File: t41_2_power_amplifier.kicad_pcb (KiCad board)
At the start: 2 copper layers, 100 x 100 mm, 2 parts, among them Q1 Q_NMOS_GSD, Q3 Q_NMOS_GSD

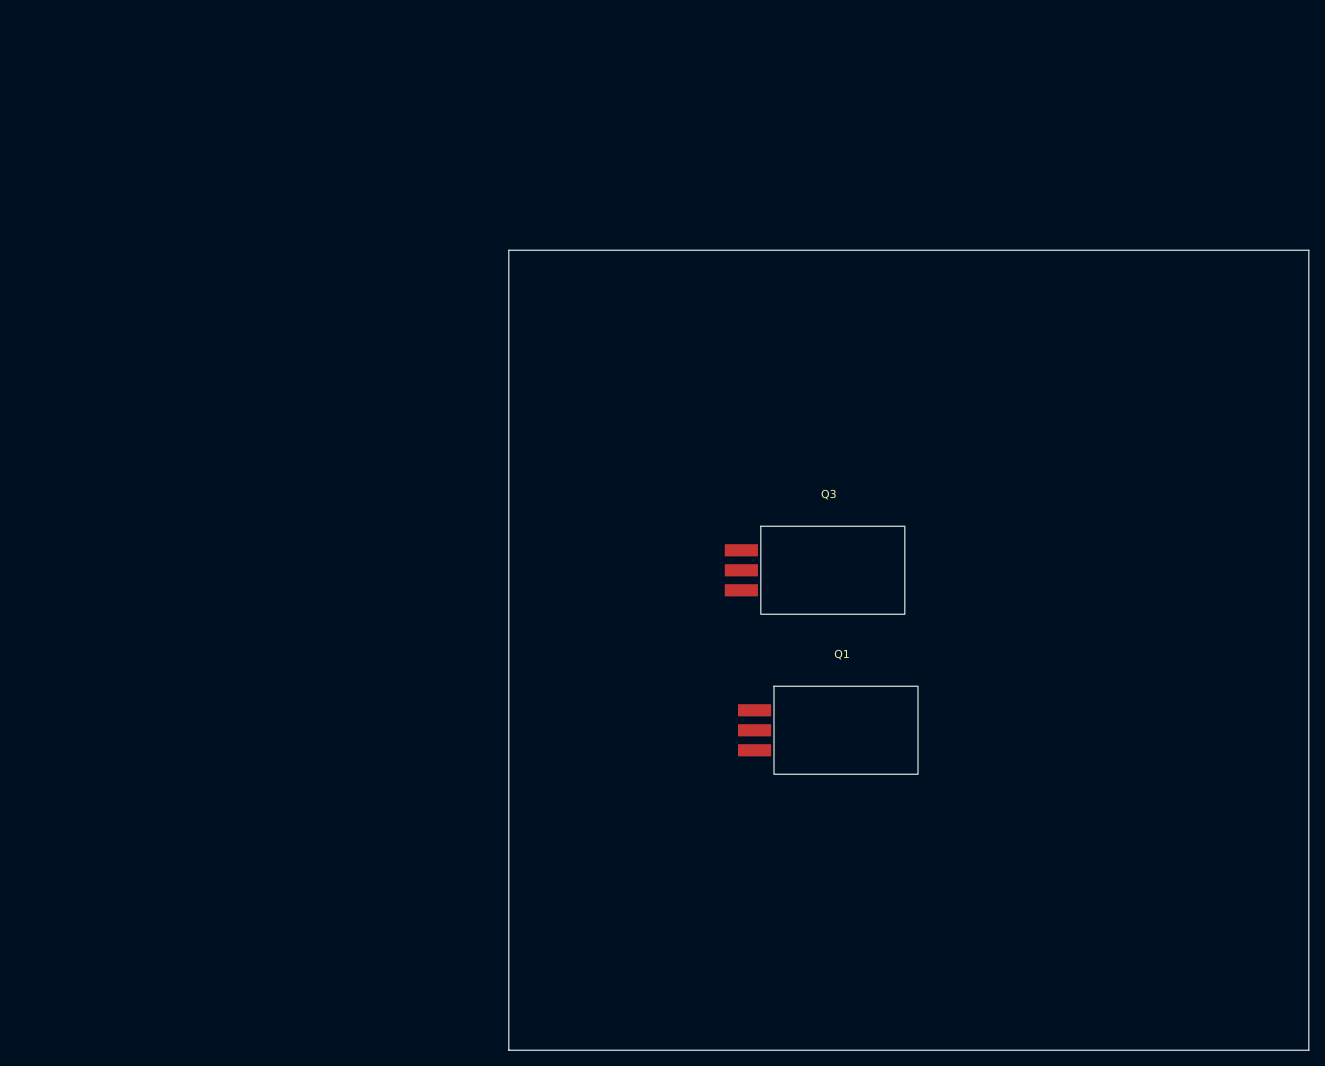
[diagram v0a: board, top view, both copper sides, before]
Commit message: Schematic complete, started on layout.
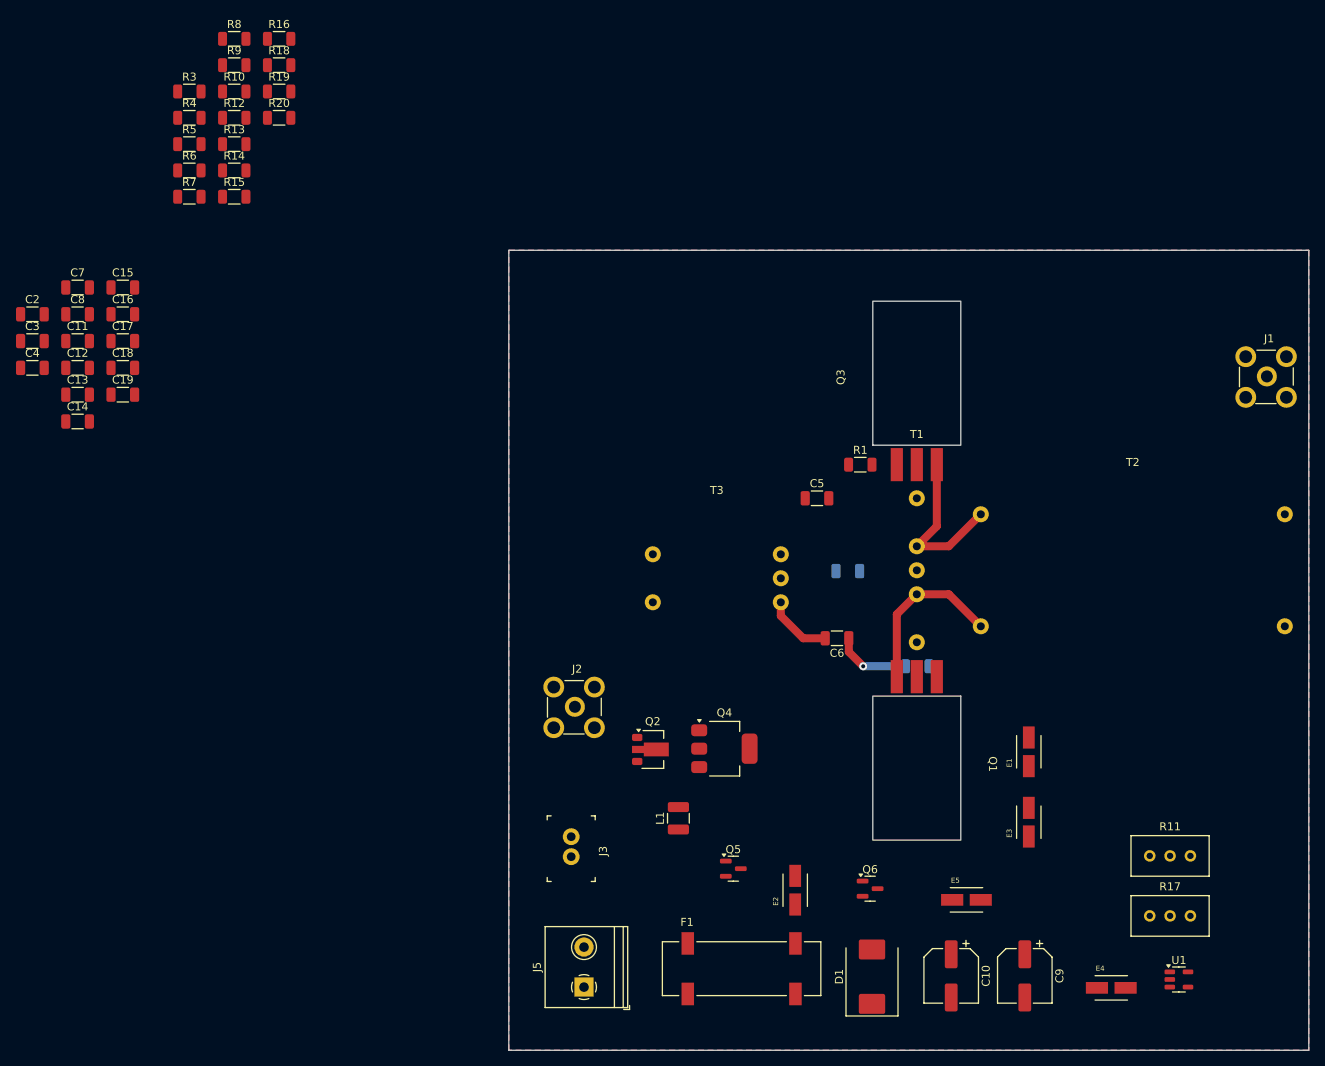
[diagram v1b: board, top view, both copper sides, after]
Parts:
- added C1: 0.1uF, Capacitor_SMD:C_1206_3216Metric, B.Cu at (142.4, 90.1)
- added C10: 47uF, Capacitor_SMD:CP_Elec_6.3x5.7, F.Cu at (155.3, 140.7)
- added C11: 0.1uF, Capacitor_SMD:C_1206_3216Metric, F.Cu at (46.1, 61.4)
- added C12: 0.1uF, Capacitor_SMD:C_1206_3216Metric, F.Cu at (46.1, 64.7)
- added C13: 0.1uF, Capacitor_SMD:C_1206_3216Metric, F.Cu at (46.1, 68.0)
- added C14: 0.1uF, Capacitor_SMD:C_1206_3216Metric, F.Cu at (46.1, 71.4)
- added C15: 0.1uF, Capacitor_SMD:C_1206_3216Metric, F.Cu at (51.8, 54.6)
- added C16: 0.1uF, Capacitor_SMD:C_1206_3216Metric, F.Cu at (51.8, 58.0)
- added C17: 0.1uF, Capacitor_SMD:C_1206_3216Metric, F.Cu at (51.8, 61.4)
- added C18: 1uF, Capacitor_SMD:C_1206_3216Metric, F.Cu at (51.8, 64.7)
- added C19: 0.1uF, Capacitor_SMD:C_1206_3216Metric, F.Cu at (51.8, 68.0)
- added C2: 180pF, Capacitor_SMD:C_1206_3216Metric, F.Cu at (40.5, 58.0)
- added C3: 0.1uF, Capacitor_SMD:C_1206_3216Metric, F.Cu at (40.5, 61.4)
- added C4: 0.1uF, Capacitor_SMD:C_1206_3216Metric, F.Cu at (40.5, 64.7)
- added C5: 0.1uF, Capacitor_SMD:C_1206_3216Metric, F.Cu at (138.5, 81.0)
- added C6: 0.1uF, Capacitor_SMD:C_1206_3216Metric, F.Cu at (141.0, 98.5)
- added C7: 0.1uF, Capacitor_SMD:C_1206_3216Metric, F.Cu at (46.1, 54.6)
- added C8: 0.1uF, Capacitor_SMD:C_1206_3216Metric, F.Cu at (46.1, 58.0)
- added C9: 47uF, Capacitor_SMD:CP_Elec_6.3x5.7, F.Cu at (164.5, 140.7)
- added D1: Z3SMCxxx, Diode_SMD:D_SMC, F.Cu at (145.4, 140.8)
- added E1: 28F0121-0SR-10, 28F0121_0SR_10:FB_28F0121-0SR-10, F.Cu at (165.0, 112.7)
- added E2: 28F0121-0SR-10, 28F0121_0SR_10:FB_28F0121-0SR-10, F.Cu at (135.8, 130.0)
- added E3: 28F0121-0SR-10, 28F0121_0SR_10:FB_28F0121-0SR-10, F.Cu at (165.0, 121.5)
- added E4: 28F0121-0SR-10, 28F0121_0SR_10:FB_28F0121-0SR-10, F.Cu at (175.3, 142.2)
- added E5: 28F0121-0SR-10, 28F0121_0SR_10:FB_28F0121-0SR-10, F.Cu at (157.2, 131.2)
- added F1: 3587TR, 3587TR:FUSE_3587TR, F.Cu at (129.1, 139.8)
- added J1: 5-1814832-1, digikey-footprints:RF_SMA_Vertical_5-1814832-1, F.Cu at (194.7, 65.8)
- added J2: 5-1814832-1, digikey-footprints:RF_SMA_Vertical_5-1814832-1, F.Cu at (108.2, 107.1)
- added J3: B2B-XH-A_LF__SN_, digikey-footprints:PinHeader_1x2_P2.5mm_Drill1.1mm, F.Cu at (107.8, 123.3)
- added J5: Screw_Terminal_01x02, TerminalBlock_Philmore:TerminalBlock_Philmore_TB132_1x02_P5.00mm_Horizontal, F.Cu at (109.4, 142.1)
- added L1: 10uH, Inductor_SMD:L_1210_3225Metric, F.Cu at (121.2, 121.0)
- added Q2: Q_NPN_BCE, Package_TO_SOT_SMD:SOT-89-3, F.Cu at (118.0, 112.4)
- added Q4: Q_NPN_BCE, Package_TO_SOT_SMD:SOT-223, F.Cu at (127.0, 112.3)
- added Q5: PMOS, Package_TO_SOT_SMD:SOT-23, F.Cu at (128.1, 127.3)
- added Q6: Q_NPN_BCE, Package_TO_SOT_SMD:SOT-23, F.Cu at (145.2, 129.8)
- added R1: 1, Resistor_SMD:R_1206_3216Metric, F.Cu at (143.9, 76.8)
- added R10: 56, Resistor_SMD:R_1206_3216Metric, F.Cu at (65.7, 30.1)
- added R11: 2k, Potentiometer_THT:Potentiometer_Bourns_3296W_Vertical, F.Cu at (185.2, 125.7)
- added R12: 56, Resistor_SMD:R_1206_3216Metric, F.Cu at (65.7, 33.4)
- added R13: 56, Resistor_SMD:R_1206_3216Metric, F.Cu at (65.7, 36.7)
- added R14: 56, Resistor_SMD:R_1206_3216Metric, F.Cu at (65.7, 40.0)
- added R15: 56, Resistor_SMD:R_1206_3216Metric, F.Cu at (65.7, 43.3)
- added R16: 56, Resistor_SMD:R_1206_3216Metric, F.Cu at (71.3, 23.6)
- added R17: 2k, Potentiometer_THT:Potentiometer_Bourns_3296W_Vertical, F.Cu at (185.2, 133.2)
- added R18: 56, Resistor_SMD:R_1206_3216Metric, F.Cu at (71.3, 26.9)
- added R19: 10k, Resistor_SMD:R_1206_3216Metric, F.Cu at (71.3, 30.1)
- added R2: 1, Resistor_SMD:R_1206_3216Metric, B.Cu at (151.1, 102.0)
- added R20: 10k, Resistor_SMD:R_1206_3216Metric, F.Cu at (71.3, 33.4)
- added R3: DNP, Resistor_SMD:R_1206_3216Metric, F.Cu at (60.1, 30.1)
- added R4: DNP, Resistor_SMD:R_1206_3216Metric, F.Cu at (60.1, 33.4)
- added R5: 56, Resistor_SMD:R_1206_3216Metric, F.Cu at (60.1, 36.7)
- added R6: 56, Resistor_SMD:R_1206_3216Metric, F.Cu at (60.1, 40.0)
- added R7: 56, Resistor_SMD:R_1206_3216Metric, F.Cu at (60.1, 43.3)
- added R8: 56, Resistor_SMD:R_1206_3216Metric, F.Cu at (65.7, 23.6)
- added R9: 56, Resistor_SMD:R_1206_3216Metric, F.Cu at (65.7, 26.9)
- added T1: Transformer_1P_SS, Binocular_Core:BN-43-202_VERTICAL, F.Cu at (151.0, 90.0)
- added T2: Transformer_1P_1S, Binocular_Core:BN-43-7051, F.Cu at (178.0, 90.0)
- added T3: Transformer_1P_SS, Binocular_Core:BN-43-302, F.Cu at (126.0, 91.0)
- added U1: MCP1802x-xx02xOT, Package_TO_SOT_SMD:SOT-23-5, F.Cu at (183.8, 141.2)
- moved Q3 26.5 mm to (151.0, 65.9), turned to 90 degrees
- moved Q1 10.3 mm to (151.0, 114.2), turned to -90 degrees
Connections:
- Q1 pad 1: unconnected-(Q1-G-Pad1) -> Net-(Q1-G)
- Q1 pad 2: unconnected-(Q1-S-Pad2) -> GND
- Q1 pad 3: unconnected-(Q1-D-Pad3) -> Net-(Q1-D)
- Q3 pad 1: unconnected-(Q3-G-Pad1) -> Net-(Q3-G)
- Q3 pad 2: unconnected-(Q3-S-Pad2) -> GND
- Q3 pad 3: unconnected-(Q3-D-Pad3) -> Net-(Q3-D)
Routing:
- net Net-(Q1-D): track 0.00 -> 21.0 mm
- net Net-(Q3-D): track 0.00 -> 20.9 mm
- net Net-(C6-Pad1): track 0.00 -> 9.55 mm, vias 0 -> 1
- net Net-(T3-SA): track 0.00 -> 8.41 mm
- added copper zone on B.Cu, net GND
- added copper zone on F.Cu, net GND
